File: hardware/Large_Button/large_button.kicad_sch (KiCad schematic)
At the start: 8 parts, among them J1 JST XH, SW1 Choc V1/V2, SW2 Choc V1/V2, SW3 Choc V1/V2

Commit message: insert summary here
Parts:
- SW1, SW2, SW3: value Choc V1/V2 -> Cherry MX; footprint PCM_Switch_Keyboard_Kailh:SW_Kailh_Choc_V1V2 -> Button_Switch_Keyboard:SW_Cherry_MX_1.00u_PCB
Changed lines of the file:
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@@
 			)
 		)
-		(property "Value" "Choc V1/V2"
+		(property "Value" "Cherry MX"
 			(at 139.7 83.82 0)
 			(effects
@@
 			)
 		)
-		(property "Footprint" "PCM_Switch_Keyboard_Kailh:SW_Kailh_Choc_V1V2"
+		(property "Footprint" "Button_Switch_Keyboard:SW_Cherry_MX_1.00u_PCB"
 			(at 139.7 83.82 0)
 			(effects
@@
 			)
 		)
-		(property "Value" "Choc V1/V2"
+		(property "Value" "Cherry MX"
 			(at 139.7 71.12 0)
 			(effects
@@
 			)
 		)
-		(property "Footprint" "PCM_Switch_Keyboard_Kailh:SW_Kailh_Choc_V1V2"
+		(property "Footprint" "Button_Switch_Keyboard:SW_Cherry_MX_1.00u_PCB"
 			(at 139.7 71.12 0)
 			(effects
@@
 			)
 		)
-		(property "Value" "Choc V1/V2"
+		(property "Value" "Cherry MX"
 			(at 139.7 58.42 0)
 			(effects
@@
 			)
 		)
-		(property "Footprint" "PCM_Switch_Keyboard_Kailh:SW_Kailh_Choc_V1V2"
+		(property "Footprint" "Button_Switch_Keyboard:SW_Cherry_MX_1.00u_PCB"
 			(at 139.7 58.42 0)
 			(effects

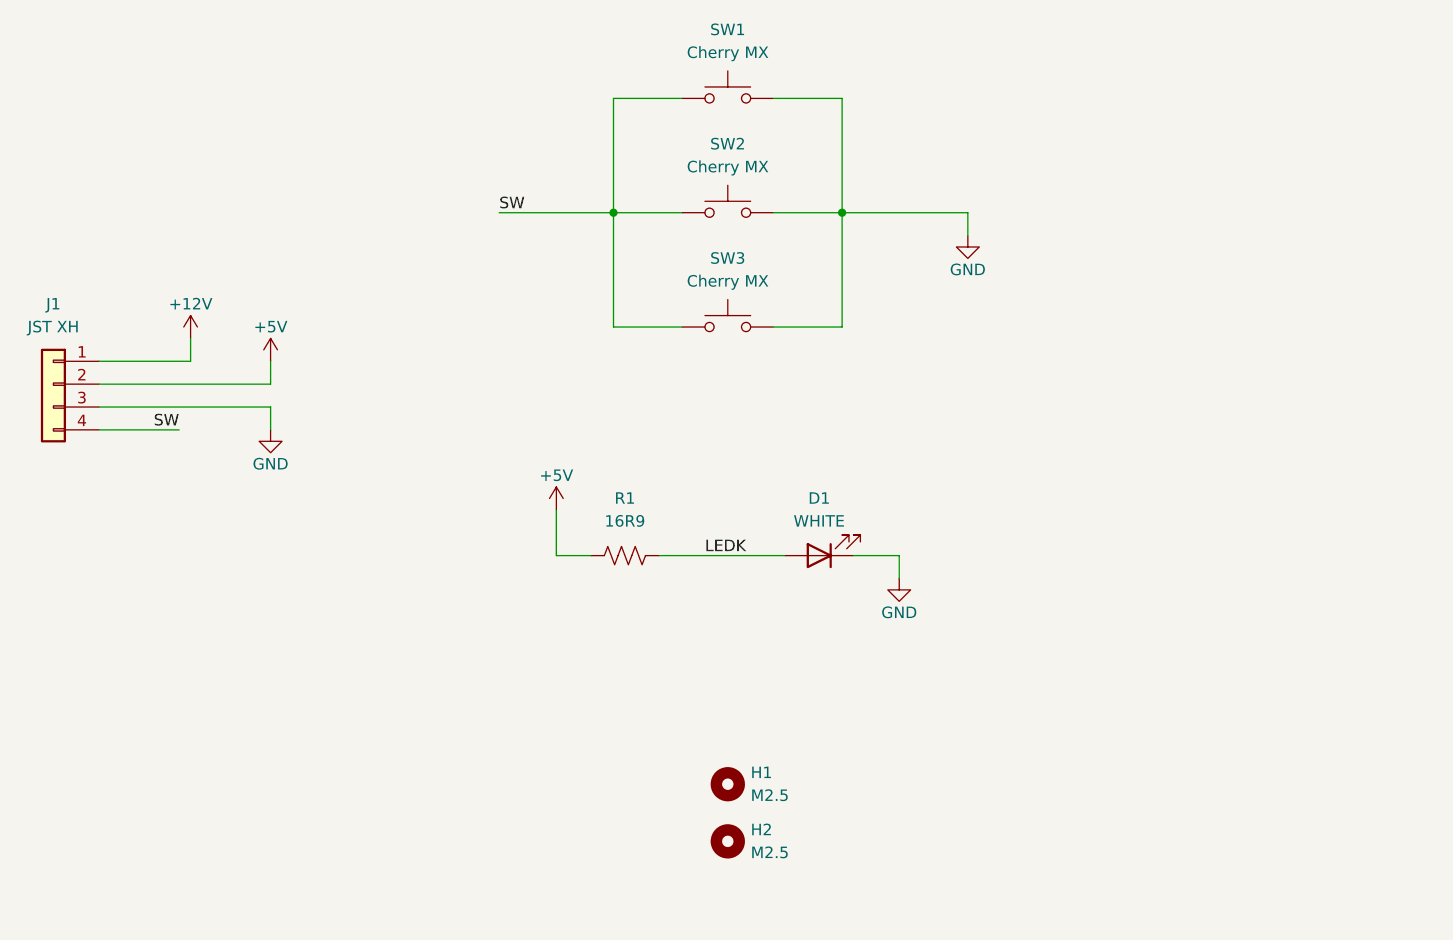
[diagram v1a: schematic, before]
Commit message: Update Large Button PCB
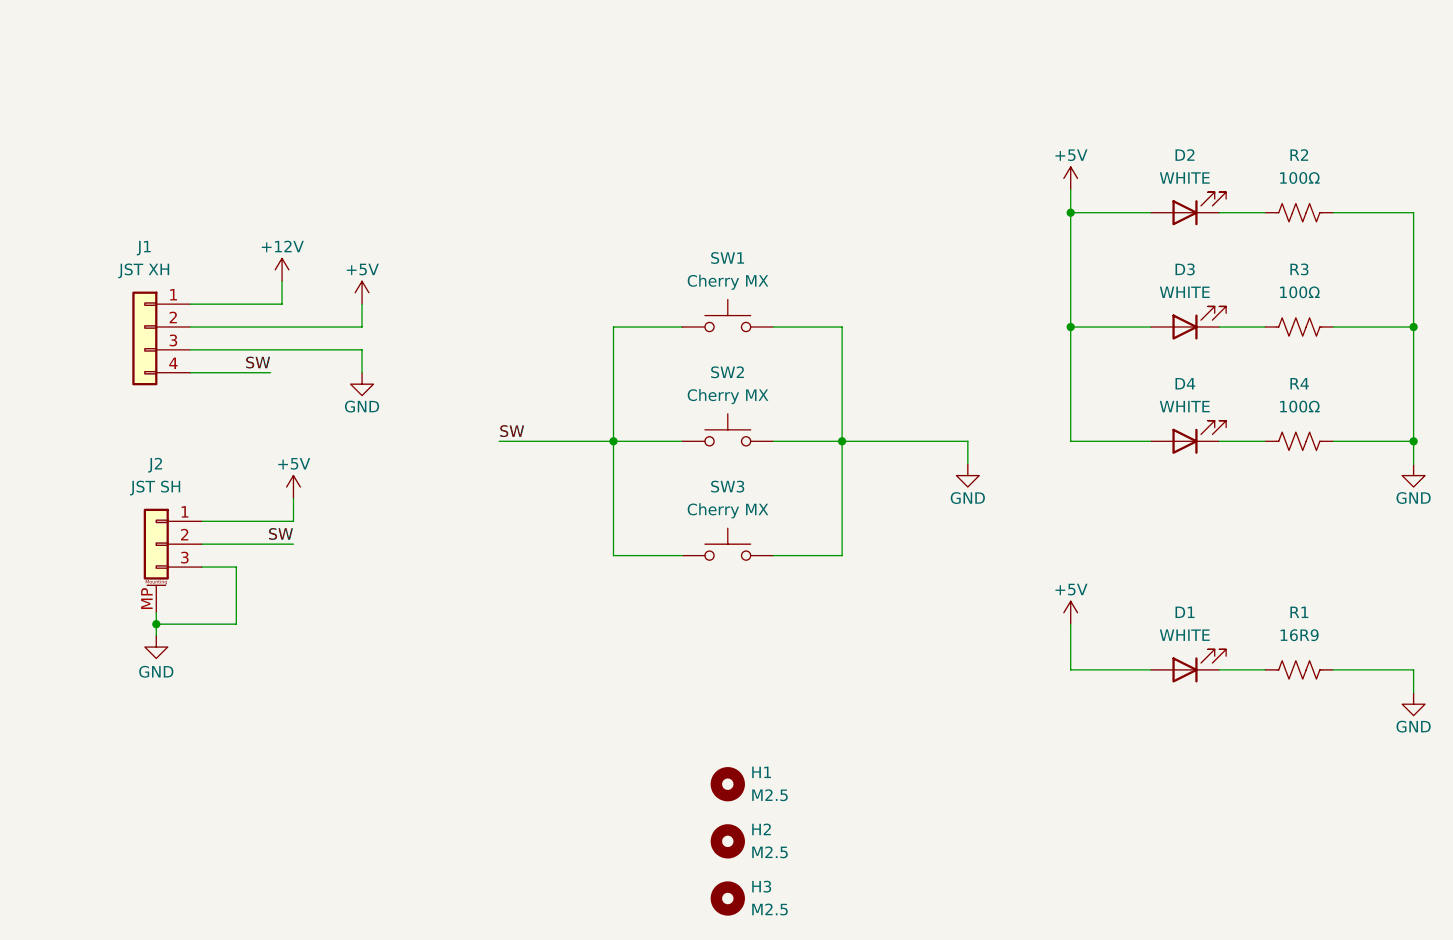
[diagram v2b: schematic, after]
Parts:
- added D2, D3, D4: WHITE, LED_THT:LED_D3.0mm, symbol Device:LED
- added H3: M2.5, MountingHole:MountingHole_2.7mm_M2.5_DIN965, symbol Mechanical:MountingHole
- added J2: JST SH, Connector_JST:JST_SH_SM03B-SRSS-TB_1x03-1MP_P1.00mm_Horizontal, symbol Connector_Generic_MountingPin:Conn_01x03_MountingPin
- added R2, R3, R4: 100Ω, Resistor_SMD:R_0402_1005Metric, symbol Device:R_US
- J1: MPN (none) -> C157925
- SW1, SW2, SW3: footprint Button_Switch_Keyboard:SW_Cherry_MX_1.00u_PCB -> UsefulModifications:SW_Cherry_MX_1.00u_PCB; now left out of the parts list
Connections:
- net +5V: now also D1.2 (A), D2.2 (A), D3.2 (A), D4.2 (A), J2.1 (Pin_1); no longer R1.1
- net GND: now also R1.2, J2.3 (Pin_3), J2.MP (MountPin), R2.2, R3.2, R4.2; no longer D1.1 (K)
- net SW: now also J2.2 (Pin_2)
- removed net LEDK: D1.2 (A), R1.2
- new net: D3.1 (K), R3.1
- new net: D1.1 (K), R1.1
- new net: D4.1 (K), R4.1
- new net: D2.1 (K), R2.1
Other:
- moved on the sheet: D1, J1, R1, SW1, SW2, SW3

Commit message: update button pcb
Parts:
- R2, R3, R4: footprint Resistor_SMD:R_0402_1005Metric -> Resistor_SMD:R_0603_1608Metric; MPN C25076 -> C22775
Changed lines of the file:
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@@
 			)
 		)
-		(property "Footprint" "Resistor_SMD:R_0402_1005Metric"
+		(property "Footprint" "Resistor_SMD:R_0603_1608Metric"
 			(at 203.454 87.884 90)
 			(effects
@@
 			)
 		)
-		(property "MPN" "C25076"
+		(property "MPN" "C22775"
 			(at 203.2 88.9 90)
 			(effects
@@
 			)
 		)
-		(property "Footprint" "Resistor_SMD:R_0402_1005Metric"
+		(property "Footprint" "Resistor_SMD:R_0603_1608Metric"
 			(at 203.454 100.584 90)
 			(effects
@@
 			)
 		)
-		(property "MPN" "C25076"
+		(property "MPN" "C22775"
 			(at 203.2 101.6 90)
 			(effects
@@
 			)
 		)
-		(property "Footprint" "Resistor_SMD:R_0402_1005Metric"
+		(property "Footprint" "Resistor_SMD:R_0603_1608Metric"
 			(at 203.454 75.184 90)
 			(effects
@@
 			)
 		)
-		(property "MPN" "C25076"
+		(property "MPN" "C22775"
 			(at 203.2 76.2 90)
 			(effects

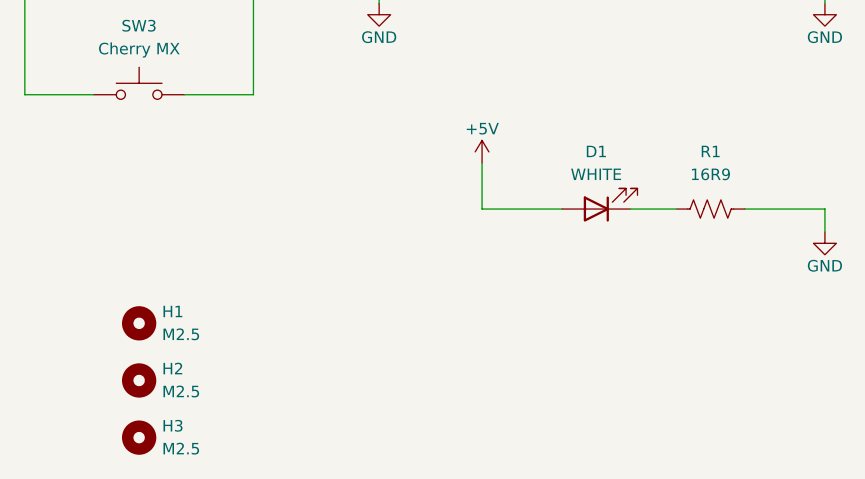
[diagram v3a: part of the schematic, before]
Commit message: Flip SMT components for Large Button PCB to bottom side
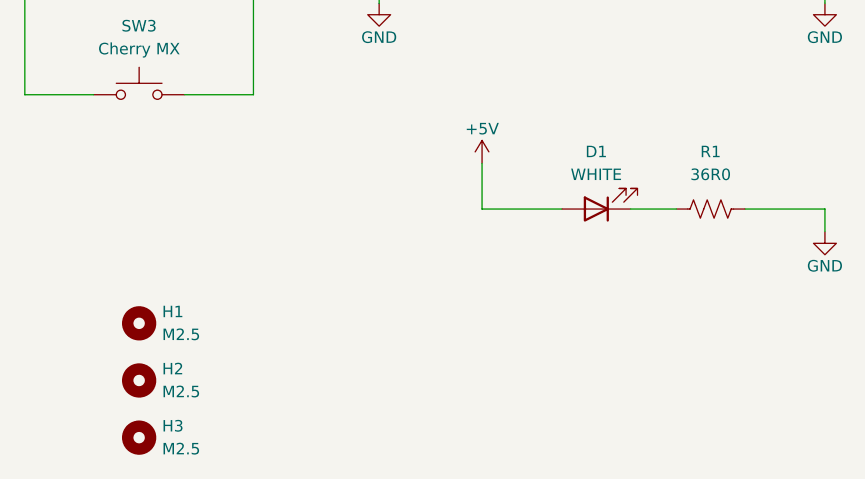
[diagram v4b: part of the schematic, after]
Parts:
- R1: value 16R9 -> 36R0; MPN C230050 -> C5121553
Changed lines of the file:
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@@
 			)
 		)
-		(property "Value" "16R9"
+		(property "Value" "36R0"
 			(at 203.2 123.19 90)
 			(effects
@@
 			)
 		)
-		(property "MPN" "C230050"
+		(property "MPN" "C5121553"
 			(at 203.2 127 90)
 			(effects
@@
 		(on_board yes)
 		(dnp no)
-		(fields_autoplaced yes)
 		(property "Reference" "H2"
 			(at 142.24 144.7799 0)
@@
 		)
 		(property "Value" "M2.5"
-			(at 142.24 147.3199 0)
-			(effects
-				(font
+			(at 142.24 147.32 0)
+			(effects
+				(font

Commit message: Big commit
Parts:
- D1, J1: now left out of the parts list
- R1: value 36R0 -> 68R0; MPN C5121553 -> C2930448
- R2, R3, R4: value 100Ω -> 150Ω; MPN C22775 -> C2907103
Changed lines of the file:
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@@
 			)
 		)
-		(property "Value" "100Ω"
+		(property "Value" "150Ω"
 			(at 203.2 85.09 90)
 			(effects
@@
 			)
 		)
-		(property "MPN" "C22775"
+		(property "MPN" "C2907103"
 			(at 203.2 88.9 90)
 			(effects
@@
 			)
 		)
-		(property "Value" "36R0"
+		(property "Value" "68R0"
 			(at 203.2 123.19 90)
 			(effects
@@
 			)
 		)
-		(property "MPN" "C5121553"
+		(property "MPN" "C2930448"
 			(at 203.2 127 90)
 			(effects
@@
 			)
 		)
-		(property "Value" "100Ω"
+		(property "Value" "150Ω"
 			(at 203.2 97.79 90)
 			(effects
@@
 			)
 		)
-		(property "MPN" "C22775"
+		(property "MPN" "C2907103"
 			(at 203.2 101.6 90)
 			(effects
@@
 		(unit 1)
 		(exclude_from_sim no)
-		(in_bom yes)
+		(in_bom no)
 		(on_board yes)
 		(dnp no)
@@
 			)
 		)
-		(property "Value" "100Ω"
+		(property "Value" "150Ω"
 			(at 203.2 72.39 90)
 			(effects
@@
 			)
 		)
-		(property "MPN" "C22775"
+		(property "MPN" "C2907103"
 			(at 203.2 76.2 90)
 			(effects
@@
 		(unit 1)
 		(exclude_from_sim no)
-		(in_bom yes)
-		(on_board yes)
-		(dnp no)
+		(in_bom no)
+		(on_board yes)
+		(dnp no)
